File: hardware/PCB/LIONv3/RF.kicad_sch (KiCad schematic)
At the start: 14 parts, among them U10 XL-1608UBC-04, U11 XL-1608UBC-04, U14 E80-900M2213S, U7 INA226AIDGSR

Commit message: feat(hardware): add ESP32-C6 UART0
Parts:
- added AE1: Antenna, symbol Device:Antenna
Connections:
- net ANT_2.4: now also AE1.1 (A)
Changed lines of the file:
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@@
+		)
+	)
+	(text_box "ANTENNA PATCH"
+		(exclude_from_sim no)
+		(at 13.97 78.74 0)
+		(size 33.02 17.78)
+		(margins 0.9525 0.9525 0.9525 0.9525)
+		(stroke
+			(width 0)
+			(type dash)
+			(color 132 0 0 1)
+		)
+		(fill
+			(type color)
+			(color 255 229 191 0.2509803922)
+		)
+		(effects
+			(font
+				(size 1.27 1.27)
+				(color 132 0 0 1)
+			)
+			(justify right bottom)
 		)
 	)
@@
 	(wire
 		(pts
+			(xy 19.05 91.44) (xy 19.05 90.17)
+		)
+		(stroke
+			(width 0)
+			(type default)
+		)
+	)
+	(wire
+		(pts
 			(xy 88.9 35.56) (xy 88.9 38.1)
 		)
@@
 		(pts
 			(xy 254 46.99) (xy 262.89 46.99)
+		)
+		(stroke
+			(width 0)
+			(type default)
+		)
+	)
+	(wire
+		(pts
+			(xy 19.05 91.44) (xy 44.45 91.44)
 		)
 		(stroke
@@
 			)
 			(justify left bottom)
+		)
+	)
+	(label "ANT_2.4"
+		(at 44.45 91.44 180)
+		(effects
+			(font
+				(size 1.27 1.27)
+			)
+			(justify right bottom)
 		)
 	)
@@
 					(unit 1)
 				)
+			)
+		)
+	)
+	(symbol
+		(lib_id "Device:Antenna")
+		(at 19.05 85.09 0)
+		(unit 1)
+		(body_style 1)
+		(exclude_from_sim no)
+		(in_bom yes)
+		(on_board yes)
+		(in_pos_files yes)
+		(dnp no)
+		(fields_autoplaced yes)
+		(property "Reference" "AE1"
+			(at 21.59 84.4549 0)
+			(show_name no)
+			(do_not_autoplace no)
+			(effects
+				(font
+					(size 1.27 1.27)
+				)
+				(justify left)
+			)
+		)
+		(property "Value" "Antenna"
+			(at 21.59 86.9949 0)
+			(show_name no)
+			(do_not_autoplace no)
+			(effects
+				(font
+					(size 1.27 1.27)
+				)
+				(justify left)
+			)
+		)
+		(property "Footprint" ""
+			(at 19.05 85.09 0)
+			(hide yes)
+			(show_name no)
+			(do_not_autoplace no)
+			(effects
+				(font
+					(size 1.27 1.27)
+				)
+			)
+		)
+		(property "Datasheet" ""
+			(at 19.05 85.09 0)
+			(hide yes)
+			(show_name no)
+			(do_not_autoplace no)
+			(effects
+				(font
+					(size 1.27 1.27)
+				)
+			)
+		)
+		(property "Description" "Antenna"
+			(at 19.05 85.09 0)
+			(hide yes)
+			(show_name no)
+			(do_not_autoplace no)
+			(effects
+				(font
+					(size 1.27 1.27)
+				)
+			)
+		)
+		(pin "1"
+		)
+		(instances
+			(project "LIONv3"
+				(path "/3cc9e06f-00d0-4bec-822f-2e156022ced4/d6030e6b-69d2-4923-80e2-2aab4b335fec"
+					(reference "AE1")
+					(unit 1)
+				)

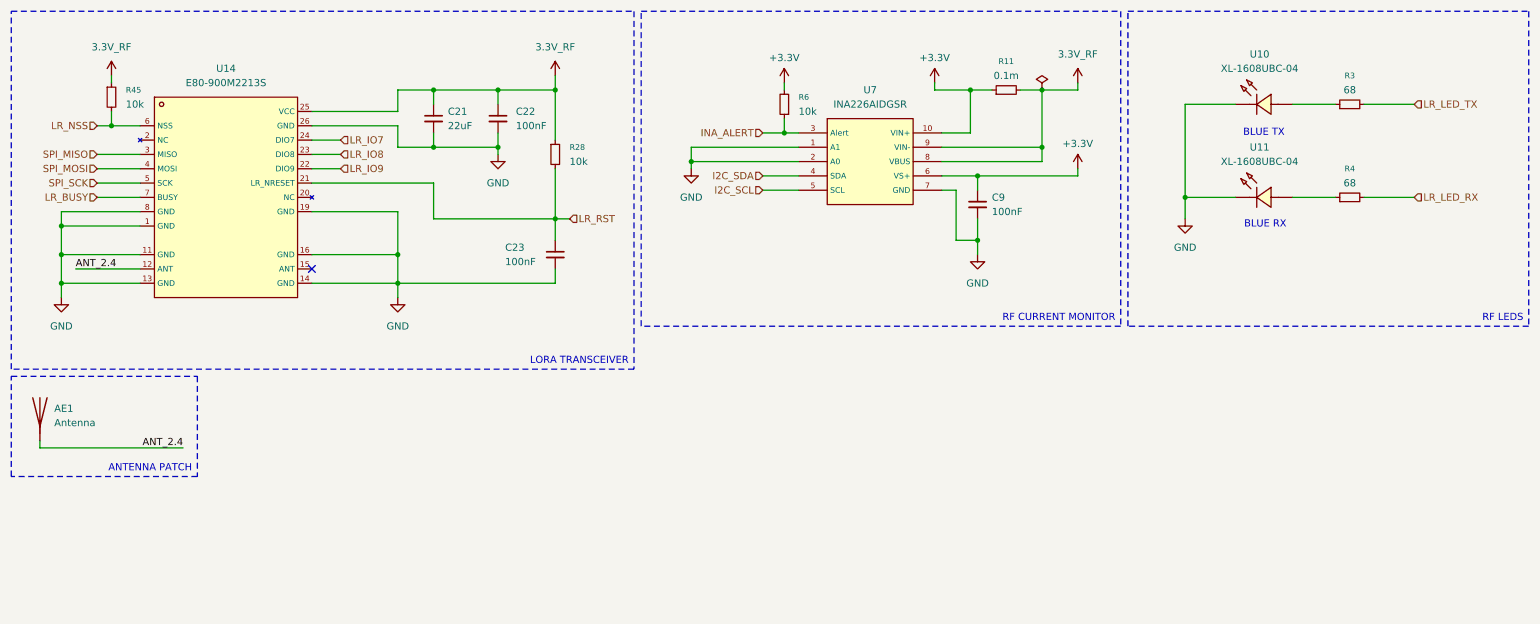
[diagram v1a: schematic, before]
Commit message: feat(hardware): finish ESP32-C6 electrical schematic
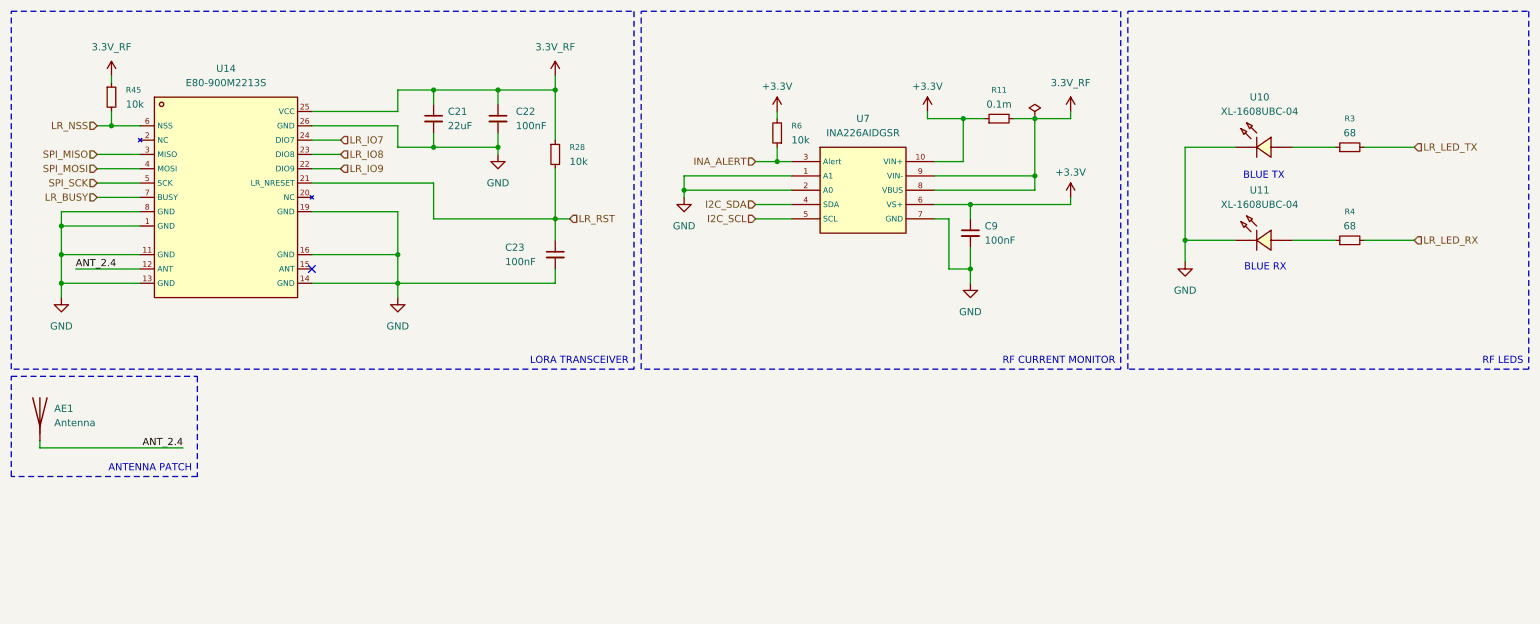
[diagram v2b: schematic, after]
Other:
- title: (none) -> LIONv3
- moved on the sheet: C9, R11, R3, R4, R6, U10, U11, U7

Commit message: feat(hardware): add MOLEX connectors
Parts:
- removed R11: 0.1m, TET-Footprints:RES-SMD_L6.3-W3.1-1, symbol Device:R_Small
- removed R4: 68, Resistor_SMD:R_0402_1005Metric, symbol Device:R_Small
- removed R6: 10k, Resistor_SMD:R_0402_1005Metric, symbol Device:R_Small
- removed U11: XL-1608UBC-04, LIONv3-Footprints:LED0603-RD_BLUE, symbol LIONv3-Symbols:XL-1608UBC-04
- added C13: 100nF, Capacitor_SMD:C_0402_1005Metric, symbol Device:C_Small
- added R12: 50m, LIONv3-Footprints:R1206, symbol Device:R_Small
- added R13, R15, R16: 10k, Resistor_SMD:R_0402_1005Metric, symbol Device:R_Small
- added U8: W25Q16JVSSIQTR, LIONv3-Footprints:SOIC-8_L5.3-W5.3-P1.27-LS8.0-BL, symbol LIONv3-Symbols:W25Q16JVSSIQTR
- AE1: now left out of the parts list
- C10: renamed from C22; LCSC (none) -> C307331
- C11: renamed from C23; LCSC (none) -> C307331
- C12: renamed from C9; LCSC (none) -> C307331
- C9: renamed from C21; LCSC (none) -> C45783
- R10: renamed from R45; LCSC (none) -> C25744
- R11: renamed from R28; LCSC (none) -> C25744
- R14: renamed from R3; LCSC (none) -> C2909380
- renumbered U14 to U5, U7 to U6, U10 to U7
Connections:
- net +3.3V: now also C13.1, R12.1, R13.1, R15.1, R16.1, U8.8 (VCC)
- net 3.3V_RF: now also R12.2
- net GND: now also C13.2, U8.4 (GND)
- net SPI_MISO: now also U8.2 (DO/IO1)
- net SPI_MOSI: now also U8.5 (DI/IO0)
- net SPI_SCK: now also U8.6 (CLK)
- net INA_ALERT: no longer names the net of U6.3 (Alert)
- net LR_IO7: no longer names the net of U5.24 (DIO7)
- net LR_IO8: no longer names the net of U5.23 (DIO8)
- net LR_IO9 renamed LR_IRQ
- net LR_LED_TX renamed LR_LED
- new net: R16.2, U8.3 (IO2)
- new net: R15.2, U8.7 (IO3)
- new net FLASH_CS: R13.2, U8.1 (/CS)
- no-connect marks 1 -> 4
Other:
- note added: "BLUE RX/TX"
- note removed: "BLUE RX"
- note removed: "BLUE TX"

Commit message: feat(hardware): finish board schematic
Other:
- note added: "VALIDATED"
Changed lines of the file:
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@@
 		(rev "0.1")
 		(comment 1 "v3-Rodrigo")
-		(comment 2 "Rodrigo")
+		(comment 2 "Rodrigo Andrade")
 		(comment 3 "2026-08-12")
 	)
@@
 		(exclude_from_sim no)
 		(at 236.22 43.18 0)
+		(effects
+			(font
+				(size 1.27 1.27)
+			)
+		)
+	)
+	(text "VALIDATED"
+		(exclude_from_sim no)
+		(at 118.11 16.51 0)
+		(effects
+			(font
+				(size 1.27 1.27)
+			)
+		)
+	)
+	(text "VALIDATED"
+		(exclude_from_sim no)
+		(at 276.86 81.28 0)
+		(effects
+			(font
+				(size 1.27 1.27)
+			)
+		)
+	)
+	(text "VALIDATED"
+		(exclude_from_sim no)
+		(at 204.47 16.51 0)
+		(effects
+			(font
+				(size 1.27 1.27)
+			)
+		)
+	)
+	(text "VALIDATED"
+		(exclude_from_sim no)
+		(at 276.86 16.51 0)
 		(effects
 			(font
@@
 			)
 		)
-		(property "Datasheet" "https://item.szlcsc.com/63461.html"
+		(property "Datasheet" "https://www.lcsc.com/datasheet/C131025.pdf"
 			(at 236.474 104.013 0)
 			(hide yes)

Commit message: feat(hardware): add TPS259474ARPWR PCB circuit
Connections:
- net ANT_2.4: no longer U5.12 (ANT)
- net ANT_915: now reaches U5.15 (ANT)
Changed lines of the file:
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@@
+	)
+	(no_connect
+		(at 36.83 59.69)
 	)
 	(no_connect
 		(at 152.4 40.64)
 	)
-	(no_connect
-		(at 67.31 59.69)
-	)
 	(wire
 		(pts
@@
 	(wire
 		(pts
-			(xy 25.4 59.69) (xy 36.83 59.69)
-		)
-		(stroke
-			(width 0)
-			(type default)
-		)
-	)
-	(wire
-		(pts
 			(xy 184.15 55.88) (xy 184.15 59.69)
 		)
@@
 	(wire
 		(pts
+			(xy 67.31 59.69) (xy 77.47 59.69)
+		)
+		(stroke
+			(width 0)
+			(type default)
+		)
+	)
+	(wire
+		(pts
 			(xy 176.53 33.02) (xy 176.53 31.75)
 		)
@@
 		)
 	)
-	(label "ANT_2.4"
-		(at 25.4 59.69 0)
+	(label "ANT_915"
+		(at 77.47 59.69 180)
 		(effects
 			(font
 				(size 1.27 1.27)
 			)
-			(justify left bottom)
-		)
-	)
+			(justify right bottom)
+		)
+	)

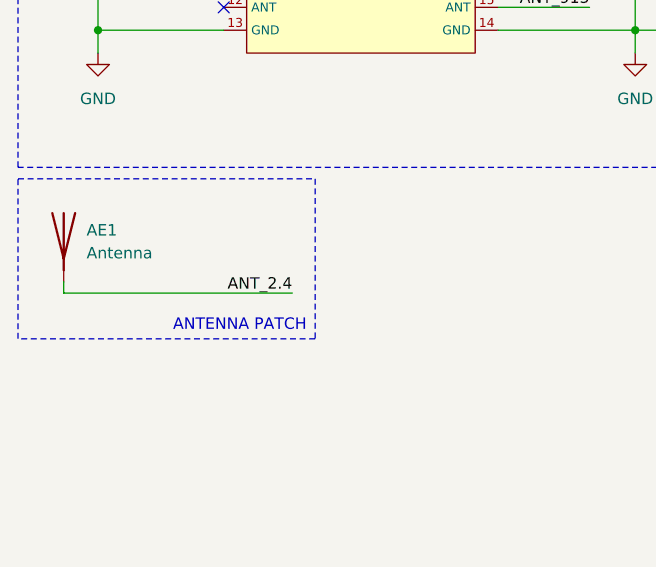
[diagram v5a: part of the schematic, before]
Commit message: feat(hardware): add TLV76733DRVR circuit
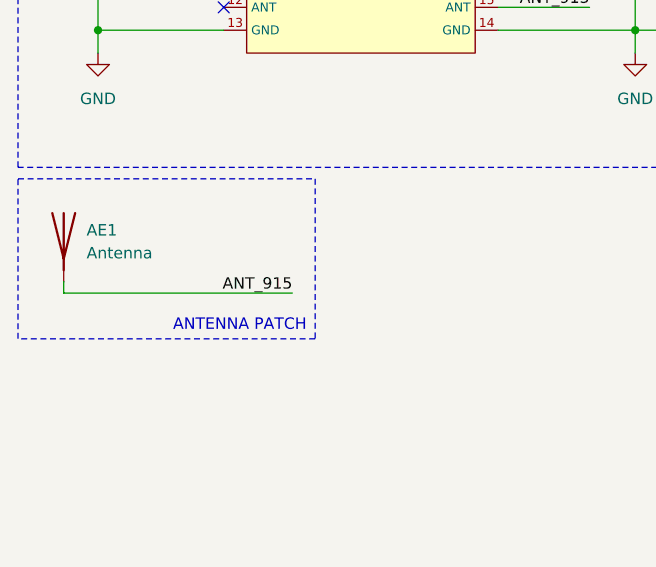
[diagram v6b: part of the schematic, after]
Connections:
- net ANT_2.4 is gone; now on net ANT_915: AE1.1 (A)
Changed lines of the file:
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@@
 		)
 	)
-	(label "ANT_2.4"
+	(label "ANT_915"
 		(at 44.45 91.44 180)
 		(effects
